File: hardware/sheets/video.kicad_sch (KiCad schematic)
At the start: 46 parts, among them J1 HDMI_A, J2 VGA HD15, M1 Core2350B (8MB PSRAM), U2 74LVC245A, U3 74LVC245A, U4 74LVC245A, U5 74LVC245A, U6 74LVC245A, U7 74LVC245A

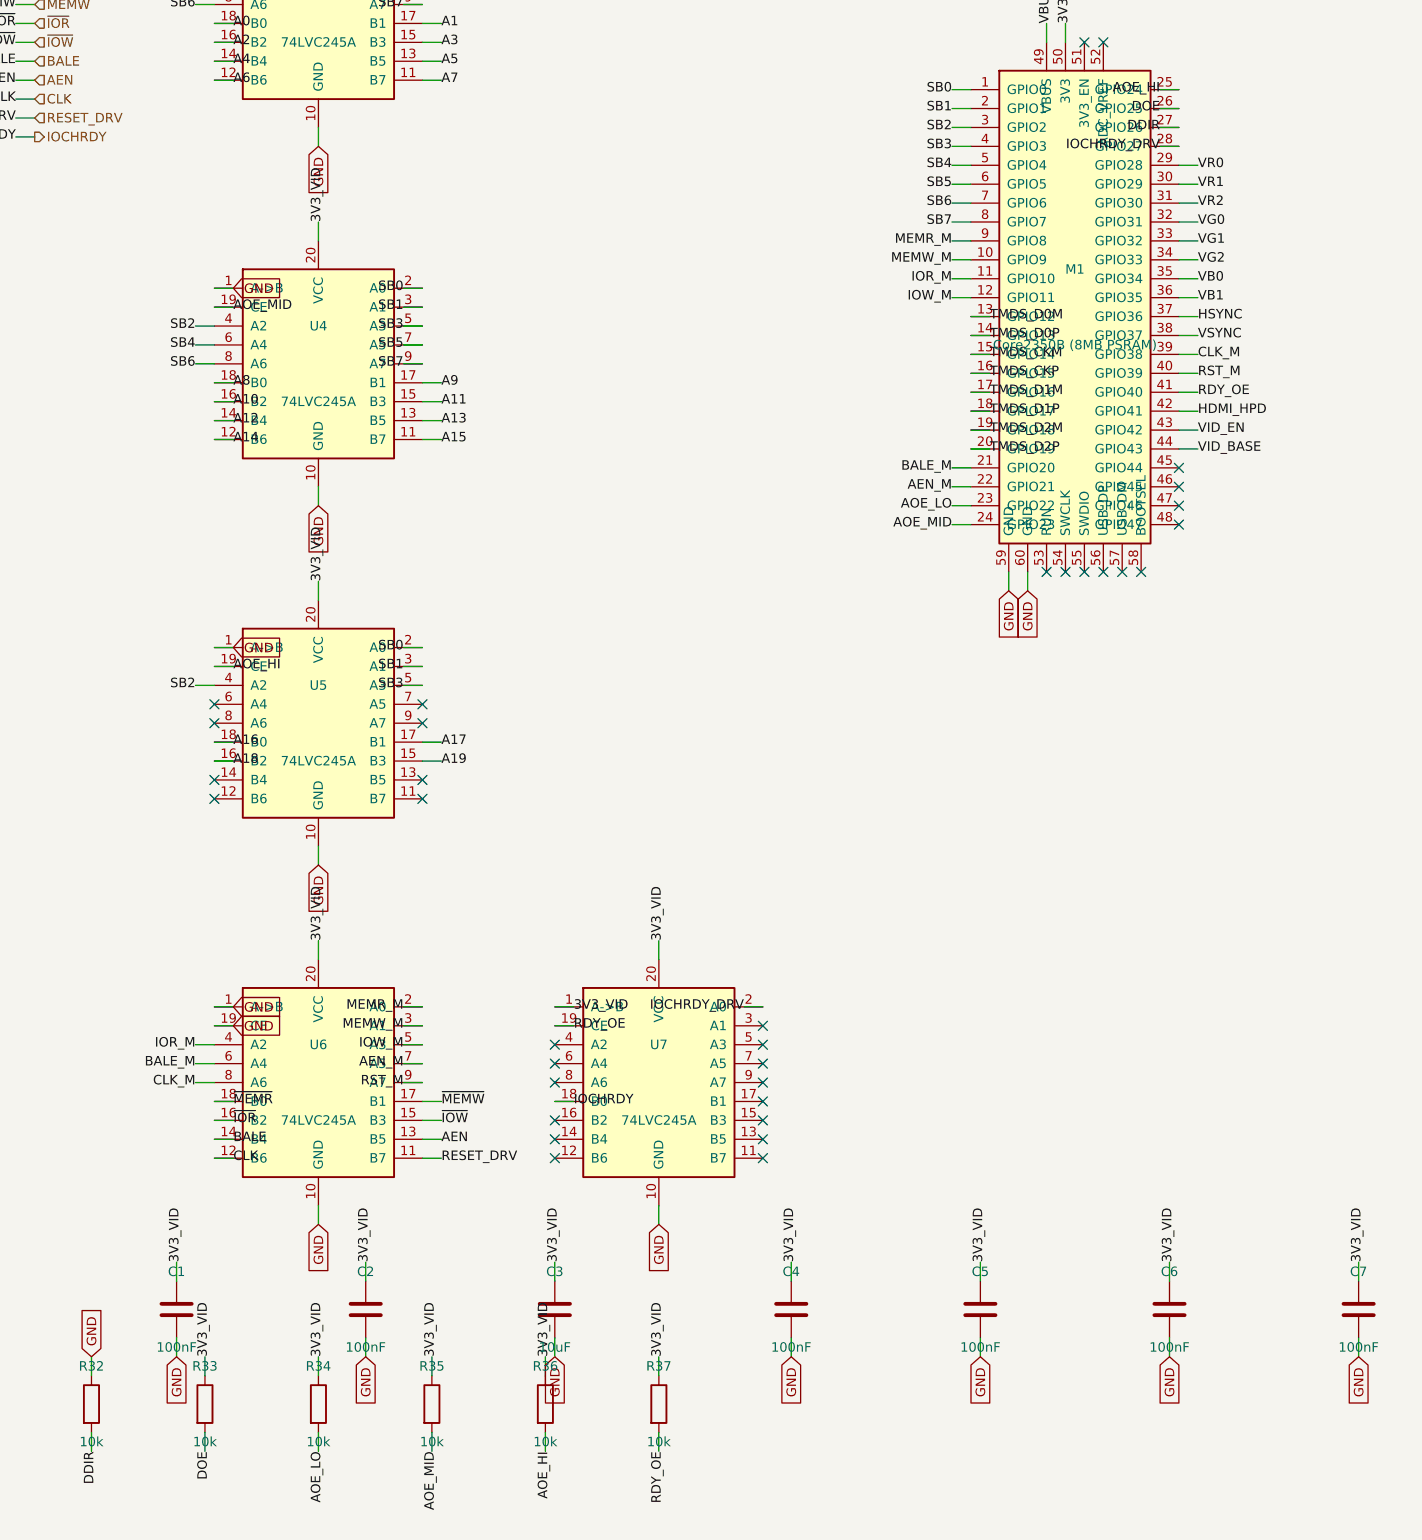
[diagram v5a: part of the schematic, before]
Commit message: video/picogus/audio: MCUs direct on 3.3V bus, shifters deleted
video.py: deleted U6 (control snoop) and U7 (IOCHRDY driver) -- pure
fixed-direction 74LVC245A buffers with nothing left to do once the ISA
bus is 3.3V-native. GPIO8-11/20/21/38/39 now label directly onto
~{MEMR}/~{MEMW}/~{IOR}/~{IOW}/BALE/AEN/CLK/RESET_DRV; GPIO27 drives
IOCHRDY directly (native tri-state); GPIO40 freed. Kept U2-U5: they are
a GPIO-budget time-division mux sharing one 8-bit snoop bus across
D0-7/A0-19, not a voltage bridge -- deleting them would need 28 GPIO
this 48-pin part doesn't have (questions-video.md #10).

picogus.py: deleted U6 (CB3T3245) -- pure fixed-direction buffering
for A8/A9/TC/IRQ5/DRQ with no muxing role; GPIO17/18/31/32/34 now
direct on those nets (gpio_map updated, mapping table preserved exactly
per 3v3-verification.md check 6). Kept U4/U5 (CB3T3257 GPIO-budget
mux) and U7/U8/U9/U10 (real Schmitt/NAND/latch/open-drain logic, never
level shifters -- already ran on 3V3_PGUS). Also fixed R9's DACK
pull-up from +5V to 3V3_PGUS: it fed 3.3V-domain gate inputs one hop
from RP2040 GPIO6/7 and had no business parking at 5V post-redesign.

audio.py: no shifter exists on this sheet (grep LVC matches only a
comment) -- pure analog summer, nothing to change. Logged as a no-op
finding.

Validated each sheet (zero structural ERC); full build exits 0.

Co-Authored-By: Claude Fable 5 <noreply@anthropic.com>
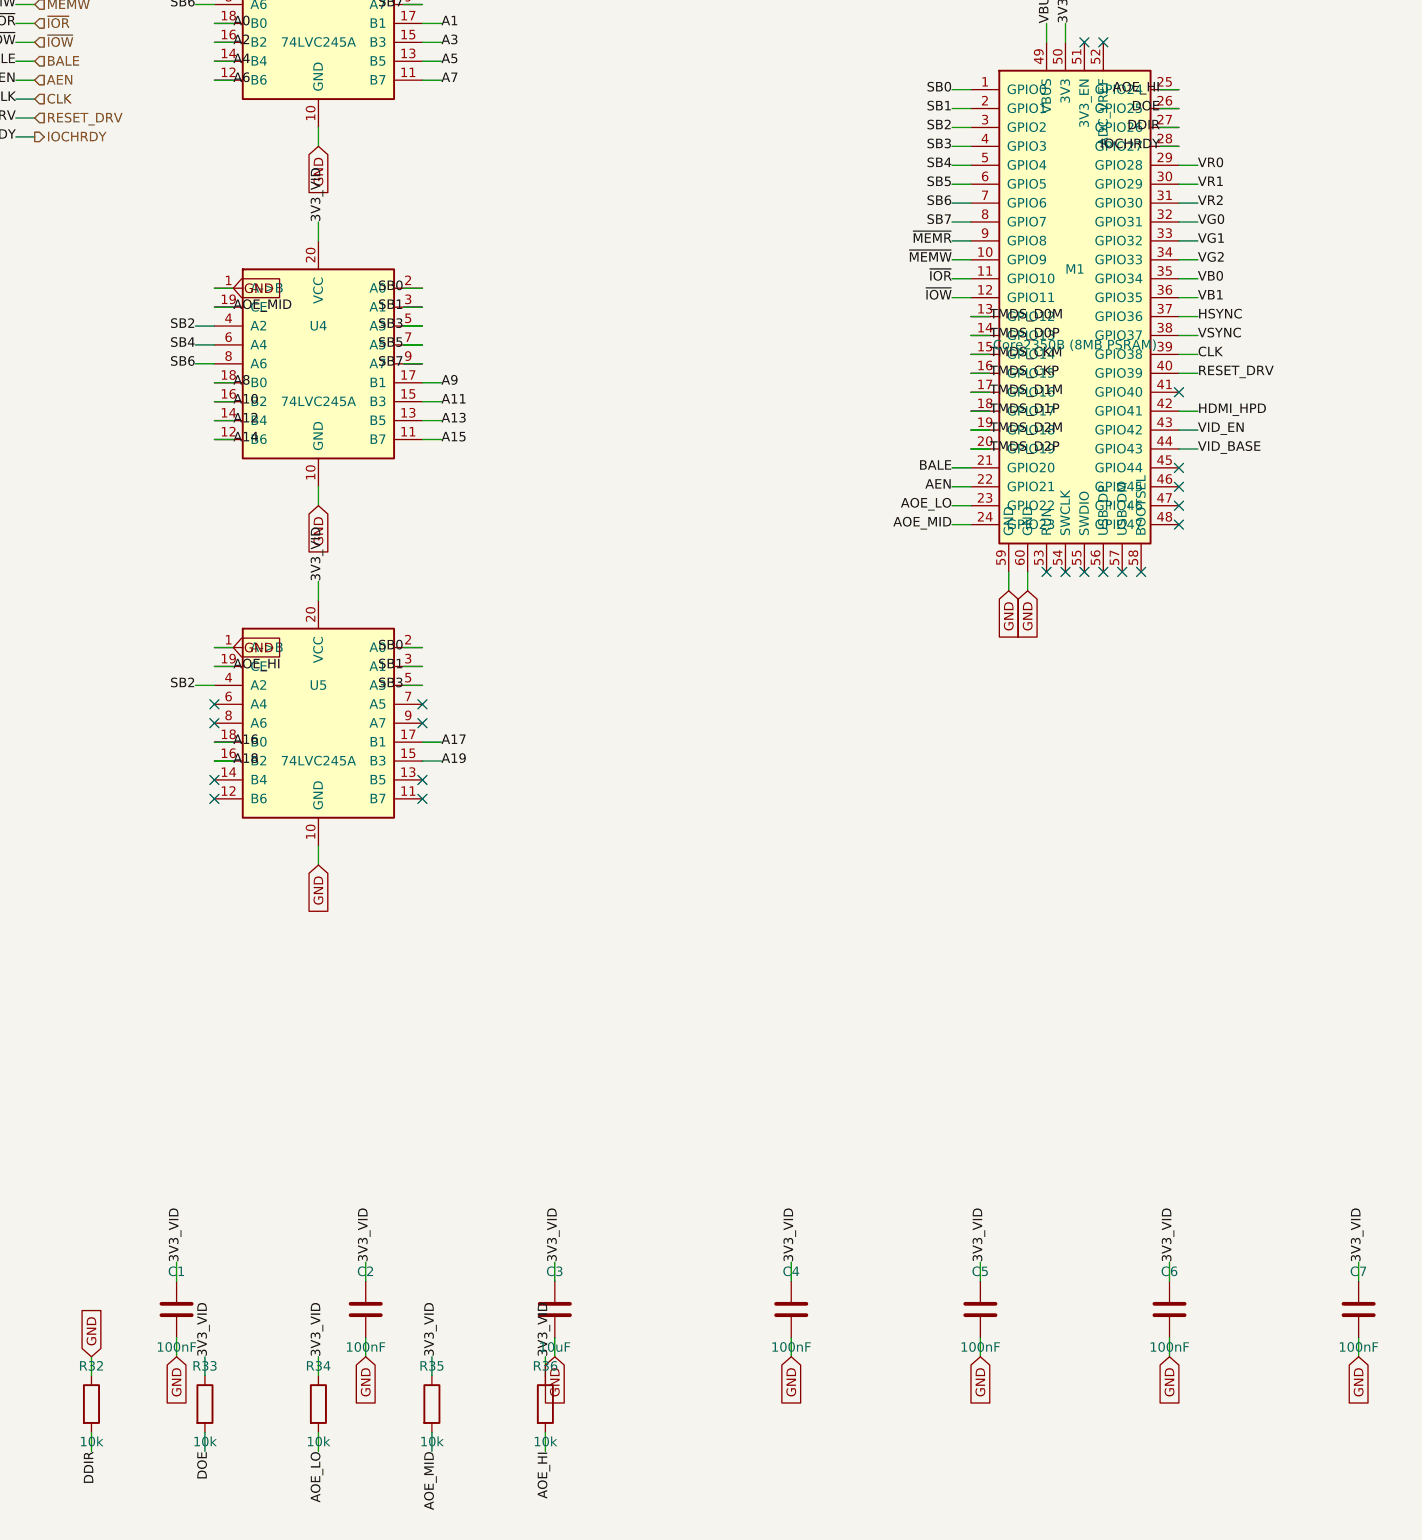
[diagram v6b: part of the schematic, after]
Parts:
- removed R10: 270, Resistor_SMD:R_0603_1608Metric, symbol Device:R
- removed R21: 1k, Resistor_SMD:R_0603_1608Metric, symbol Device:R
- removed R28: 100, Resistor_SMD:R_0603_1608Metric, symbol Device:R
- removed R37: 10k, Resistor_SMD:R_0603_1608Metric, symbol Device:R
- removed U7: 74LVC245A, Package_SO:TSSOP-20_4.4x6.5mm_P0.65mm, symbol mini-xt:74LVC245A
- added R11, R16: 270, Resistor_SMD:R_0603_1608Metric, symbol Device:R
- R10: renamed from U6; value 74LVC245A -> 270; footprint Package_SO:TSSOP-20_4.4x6.5mm_P0.65mm -> Resistor_SMD:R_0603_1608Metric; symbol mini-xt:74LVC245A -> Device:R; LCSC Part Num C6082 -> C22966
- R21: renamed from R11; value 270 -> 1k; LCSC Part Num C22966 -> C21190
- R28: renamed from R16; value 270 -> 100; LCSC Part Num C22966 -> C22775
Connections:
- net IOCHRDY_DRV is gone; now on net IOCHRDY: M1.28 (GPIO27)
- net 3V3_VID: no longer R10.20 (VCC)
- net AEN: now also M1.22 (GPIO21); no longer R10.13 (B5)
- net BALE: now also M1.21 (GPIO20); no longer R10.14 (B4)
- net CLK: now also M1.39 (GPIO38); no longer R10.12 (B6)
- net GND: no longer R10.1 (A->B), R10.10 (GND), R10.19 (CE)
- net HDMI_CKP: now also R16.2; no longer R28.2
- net HDMI_D2M: now also R11.2; no longer R21.2
- net HDMI_D2P: now also R10.2
- net HSYNC: now also R28.1
- net HSYNC_J: now also R28.2
- net RESET_DRV: now also M1.40 (GPIO39); no longer R10.11 (B7)
- net TMDS_CKP: now also R16.1; no longer R28.1
- net TMDS_D2M: now also R11.1; no longer R21.1
- net TMDS_D2P: now also R10.1
- net VGA_R: now also R21.2
- net VR1: now also R21.1
- net ~{IOR}: now also M1.11 (GPIO10); no longer R10.16 (B2)
- net ~{IOW}: now also M1.12 (GPIO11); no longer R10.15 (B3)
- net ~{MEMR}: now also M1.9 (GPIO8); no longer R10.18 (B0)
- net ~{MEMW}: now also M1.10 (GPIO9); no longer R10.17 (B1)
- removed net AEN_M: M1.22 (GPIO21), R10.7 (A5)
- removed net BALE_M: M1.21 (GPIO20), R10.6 (A4)
- removed net CLK_M: M1.39 (GPIO38), R10.8 (A6)
- removed net IOR_M: M1.11 (GPIO10), R10.4 (A2)
- removed net IOW_M: M1.12 (GPIO11), R10.5 (A3)
- removed net MEMR_M: M1.9 (GPIO8), R10.2 (A0)
- removed net MEMW_M: M1.10 (GPIO9), R10.3 (A1)
- net RDY_OE: no longer names the net of M1.41 (GPIO40)
- removed net RST_M: M1.40 (GPIO39), R10.9 (A7)
- no-connect marks 43 -> 30
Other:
- moved on the sheet: R21, R28

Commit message: addr_decode: hardwire LPT/IDE bases; centralize NIC + video disables (JP1-JP6)
LPT fixed at 0x378, IDE at 0x300 -- both base straps and their pull-ups
deleted ('138 ~Y1 now NC, the '00's ~A5 gate spare, IDE OR-leg takes raw
A5). The NIC and video disable jumpers move to addr_decode as JP5/JP6
with the same fit-to-disable sense as the rest: their gating hardware
stays local (the NIC's isolation '125 inside the 5V island, video's
firmware boot strap on GPIO42), only the jumper levels cross as
mxbus.PRIV_DIS -- video's documented firmware polarity inverts (high =
disabled; no firmware exists yet). Disable row is now a uniform JP1-JP6
(COM1/COM2/LPT/IDE/NIC/VID), bare board runs everything; network JP1/R6
and video JP1/R30 deleted, VID_BASE becomes video JP1. card_video's
wrapper re-adds a local DIS_VID strap (the documented PRIV lift
pattern). Docs/tables/decision logs aligned.

Co-Authored-By: Claude Fable 5 <noreply@anthropic.com>
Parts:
- removed JP2: VID_BASE, Connector_PinHeader_2.54mm:PinHeader_1x02_P2.54mm_Vertical, symbol Connector_Generic:Conn_01x02
- removed R17: 270, Resistor_SMD:R_0603_1608Metric, symbol Device:R
- removed R30: 10k, Resistor_SMD:R_0603_1608Metric, symbol Device:R
- added R10: 270, Resistor_SMD:R_0603_1608Metric, symbol Device:R
- JP1: value VID_EN -> VID_BASE
- renumbered R10 to R11, R11 to R12, R12 to R13, R13 to R14, R14 to R15, R15 to R16, R16 to R17
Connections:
- net HDMI_CKM: now also R17.2
- net HDMI_CKP: now also R16.2; no longer R17.2
- net HDMI_D0M: now also R15.2; no longer R16.2
- net HDMI_D0P: now also R14.2; no longer R15.2
- net HDMI_D1M: now also R13.2; no longer R14.2
- net HDMI_D1P: now also R12.2; no longer R13.2
- net HDMI_D2M: now also R11.2; no longer R12.2
- net HDMI_D2P: now also R10.2; no longer R11.2
- net TMDS_CKM: now also R17.1
- net TMDS_CKP: now also R16.1; no longer R17.1
- net TMDS_D0M: now also R15.1; no longer R16.1
- net TMDS_D0P: now also R14.1; no longer R15.1
- net TMDS_D1M: now also R13.1; no longer R14.1
- net TMDS_D1P: now also R12.1; no longer R13.1
- net TMDS_D2M: now also R11.1; no longer R12.1
- net TMDS_D2P: now also R10.1; no longer R11.1
- net VID_BASE: now also JP1.1 (Pin_1)
- net VID_EN renamed DIS_VID
- net DIS_VID: no longer JP1.1 (Pin_1)
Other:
- note added: "SOFT CARD: ISA bus + power ONLY. Self-decodes 0xA0000-0xBFFFF and 3B4/3B5/3B8/3BA/3BF + 3D4/3D5/3D8/3D9/3DA from snooped A17-A19/A0-A9. No Y5, no link, no host RAM (design S8). Disable: addr_decode JP6 (DIS_VID high, firmware keeps all OEs off; enabled by default). JP1 = CGA (closed) / MDA (open) window set."
- note removed: "SOFT CARD: ISA bus + power ONLY. Self-decodes 0xA0000-0xBFFFF and 3B4/3B5/3B8/3BA/3BF + 3D4/3D5/3D8/3D9/3DA from snooped A17-A19/A0-A9. No Y5, no link, no host RAM (design S8). Straps: JP1 open = card disabled (firmware keeps all OEs off); JP2 = CGA (closed) / MDA (open) window set."
- moved on the sheet: R11, R12, R13, R14, R15, R16, R17
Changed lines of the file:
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@@
 	(wire
 		(pts
+			(xy 22.86 119.38)
+			(xy 25.4 119.38)
+		)
+		(stroke
+			(width 0)
+			(type default)
+		)
+	)
+	(label "DIS_VID"
+		(at 22.86 119.38 180)
+		(effects
+			(font
+				(size 1.27 1.27)
+			)
+			(justify right)
+		)
+	)
+	(hierarchical_label "DIS_VID"
+		(shape input)
+		(at 25.4 119.38 0)
+		(effects
+			(font
+				(size 1.27 1.27)
+			)
+		)
+	)
+	(wire
+		(pts
 			(xy 161.29 104.14)
 			(xy 161.29 101.6)
@@
 		)
 	)
-	(label "VID_EN"
+	(label "DIS_VID"
 		(at 181.61 156.21 0)
 		(effects
@@
 	(wire
 		(pts
-			(xy 116.84 40.64)
-			(xy 119.38 40.64)
-		)
-		(stroke
-			(width 0)
-			(type default)
-		)
-	)
-	(label "VID_EN"
-		(at 119.38 40.64 0)
-		(effects
-			(font
-				(size 1.27 1.27)
-			)
-		)
-	)
-	(wire
-		(pts
-			(xy 116.84 43.18)
-			(xy 119.38 43.18)
-		)
-		(stroke
-			(width 0)
-			(type default)
-		)
-	)
-	(global_label "GND"
-		(shape input)
-		(at 119.38 43.18 0)
-		(effects
-			(font
-				(size 1.27 1.27)
-			)
-		)
-	)
-	(wire
-		(pts
 			(xy 132.08 40.64)
 			(xy 134.62 40.64)
@@
 	(wire
 		(pts
-			(xy 121.92 57.15)
-			(xy 121.92 54.61)
-		)
-		(stroke
-			(width 0)
-			(type default)
-		)
-	)
-	(label "3V3_VID"
-		(at 121.92 54.61 90)
-		(effects
-			(font
-				(size 1.27 1.27)
-			)
-		)
-	)
-	(wire
-		(pts
-			(xy 121.92 64.77)
-			(xy 121.92 67.31)
-		)
-		(stroke
-			(width 0)
-			(type default)
-		)
-	)
-	(label "VID_EN"
-		(at 121.92 67.31 270)
-		(effects
-			(font
-				(size 1.27 1.27)
-			)
-		)
-	)
-	(wire
-		(pts
 			(xy 137.16 57.15)
 			(xy 137.16 54.61)
@@
 		(at 317.5 233.68)
 	)
-	(text "SOFT CARD: ISA bus + power ONLY. Self-decodes 0xA0000-0xBFFFF and 3B4/3B5/3B8/3BA/3BF + 3D4/3D5/3D8/3D9/3DA from snooped A17-A19/A0-A9. No Y5, no link, no host RAM (design S8). Straps: JP1 open = card disabled (firmware keeps all OEs off); JP2 = CGA (closed) / MDA (open) window set."
+	(text "SOFT CARD: ISA bus + power ONLY. Self-decodes 0xA0000-0xBFFFF and 3B4/3B5/3B8/3BA/3BF + 3D4/3D5/3D8/3D9/3DA from snooped A17-A19/A0-A9. No Y5, no link, no host RAM (design S8). Disable: addr_decode JP6 (DIS_VID high, firmware keeps all OEs off; enabled by default). JP1 = CGA (closed) / MDA (open) window set."
 		(at 38.1 20.32 0)
 		(effects
@@
 	(symbol
 		(lib_id "Connector_Generic:Conn_01x02")
-		(at 121.92 40.64 0)
-		(unit 1)
-		(exclude_from_sim no)
-		(in_bom yes)
-		(on_board yes)
-		(dnp no)
-		(fields_autoplaced yes)
-		(property "Reference" "JP1"
-			(at 121.92 35.56 0)
-			(effects
-				(font
-					(size 1.27 1.27)
-				)
-			)
-		)
-		(property "Value" "VID_EN"
-			(at 121.92 45.72 0)
-			(effects
-				(font
-					(size 1.27 1.27)
-				)
-			)
-		)
-		(property "Footprint" "Connector_PinHeader_2.54mm:PinHeader_1x02_P2.54mm_Vertical"
-			(at 121.92 40.64 0)
-			(effects
-				(font
-					(size 1.27 1.27)
-				)
-				(hide yes)
-			)
-		)
-		(property "LCSC Part Num" "C2337"
-			(at 121.92 40.64 0)
-			(effects
-				(font
-					(size 1.27 1.27)
-				)
-				(hide yes)
-			)
-		)
-		(pin "1"
-		)
-		(pin "2"
-		)
-		(instances
-			(project "mini-xt"
-				(path "/26736c46-8b40-5460-874f-03596d17270c/45c2b3fd-b915-52bc-9ea2-0bf3f8b1b034"
-					(reference "JP401")
-					(unit 1)
-				)
-			)
-		)
-	)
-	(symbol
-		(lib_id "Connector_Generic:Conn_01x02")
 		(at 137.16 40.64 0)
 		(unit 1)
@@
 		(dnp no)
 		(fields_autoplaced yes)
-		(property "Reference" "JP2"
+		(property "Reference" "JP1"
 			(at 137.16 35.56 0)
 			(effects
@@
 			(project "mini-xt"
 				(path "/26736c46-8b40-5460-874f-03596d17270c/45c2b3fd-b915-52bc-9ea2-0bf3f8b1b034"
-					(reference "JP402")
-					(unit 1)
-				)
-			)
-		)
-	)
-	(symbol
-		(lib_id "Device:R")
-		(at 121.92 60.96 0)
-		(unit 1)
-		(exclude_from_sim no)
-		(in_bom yes)
-		(on_board yes)
-		(dnp no)
-		(fields_autoplaced yes)
-		(property "Reference" "R30"
-			(at 121.92 55.88 0)
-			(effects
-				(font
-					(size 1.27 1.27)
-				)
-			)
-		)
-		(property "Value" "10k"
-			(at 121.92 66.04 0)
-			(effects
-				(font
-					(size 1.27 1.27)
-				)
-			)
-		)
-		(property "Footprint" "Resistor_SMD:R_0603_1608Metric"
-			(at 121.92 60.96 0)
-			(effects
-				(font
-					(size 1.27 1.27)
-				)
-				(hide yes)
-			)
-		)
-		(property "LCSC Part Num" "C25804"
-			(at 121.92 60.96 0)
-			(effects
-				(font
-					(size 1.27 1.27)
-				)
-				(hide yes)
-			)
-		)
-		(pin "1"
-		)
-		(pin "2"
-		)
-		(instances
-			(project "mini-xt"
-				(path "/26736c46-8b40-5460-874f-03596d17270c/45c2b3fd-b915-52bc-9ea2-0bf3f8b1b034"
-					(reference "R430")
+					(reference "JP401")
 					(unit 1)
 				)
